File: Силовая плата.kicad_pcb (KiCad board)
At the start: 6 copper layers, 65.7 x 72.2 mm, 57 parts, among them J3 Conn_01x01, J4 Conn_01x01, J5 Conn_01x01, J6 Conn_02x04_Odd_Even, Q1 BSP89, Q2 BSP89, Q3 BSP89, Q4 BSP89, Q5 BSP89, Q6 BSP89, U1 LMV7239M5, U6 AD8210

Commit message: Стартовая версия
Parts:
- removed C11: 56p, Capacitor_SMD:C_0805_2012Metric_Pad1.18x1.45mm_HandSolder
- removed C14, C15, C16, C17, C18, C19, C20, C21: 4.7u, Capacitor_SMD:C_1206_3216Metric_Pad1.33x1.80mm_HandSolder
- removed C2: 1400m, Capacitor_THT:CP_Axial_L30.0mm_D18.0mm_P35.00mm_Horizontal
- removed C5, C7, C9: BS, Capacitor_SMD:C_0805_2012Metric_Pad1.18x1.45mm_HandSolder
- removed C6, C8: 10u, Capacitor_SMD:C_0805_2012Metric_Pad1.18x1.45mm_HandSolder
- removed D1, D2, D5: D_Small, Diode_SMD:D_SOD-323
- removed D3, D4, D6: ADP3110A, Package_DFN_QFN:DFN-8-1EP_3x3mm_P0.65mm_EP1.7x2.05mm
- removed R13, R14, R15, R16, R17, R18: 2.7, Resistor_SMD:R_0805_2012Metric_Pad1.20x1.40mm_HandSolder
- removed R21: 10k, Resistor_SMD:R_0805_2012Metric_Pad1.20x1.40mm_HandSolder
- removed R3, R4: 120, Resistor_SMD:R_0805_2012Metric_Pad1.20x1.40mm_HandSolder
- added J7: A_CTRL, Connector_PinSocket_2.54mm:PinSocket_2x04_P2.54mm_Vertical_SMD, F.Cu at (106.0, 114.3)
- added J9: C_CTRL, Connector_PinSocket_2.54mm:PinSocket_2x04_P2.54mm_Vertical_SMD, F.Cu at (59.7, 113.7)
- added Q10: BSP89, Package_SON:VSONP-8-1EP_5x6_P1.27mm, F.Cu at (87.0, 74.9)
- added Q11: BSP89, Package_SON:VSONP-8-1EP_5x6_P1.27mm, F.Cu at (87.0, 80.6)
- added Q12: BSP89, Package_SON:VSONP-8-1EP_5x6_P1.27mm, F.Cu at (87.0, 86.4)
- added Q13: BSP89, Package_SON:VSONP-8-1EP_5x6_P1.27mm, F.Cu at (68.3, 99.7)
- added Q14: BSP89, Package_SON:VSONP-8-1EP_5x6_P1.27mm, F.Cu at (68.3, 94.0)
- added Q15: BSP89, Package_SON:VSONP-8-1EP_5x6_P1.27mm, F.Cu at (68.3, 88.3)
- added Q16: BSP89, Package_SON:VSONP-8-1EP_5x6_P1.27mm, F.Cu at (98.1, 94.0)
- added Q17: BSP89, Package_SON:VSONP-8-1EP_5x6_P1.27mm, F.Cu at (98.1, 88.3)
- added Q18: BSP89, Package_SON:VSONP-8-1EP_5x6_P1.27mm, F.Cu at (98.1, 82.5)
- added Q19: BSP89, Package_SON:VSONP-8-1EP_5x6_P1.27mm, F.Cu at (79.4, 74.9)
- added Q20: BSP89, Package_SON:VSONP-8-1EP_5x6_P1.27mm, F.Cu at (79.4, 80.6)
- added Q21: BSP89, Package_SON:VSONP-8-1EP_5x6_P1.27mm, F.Cu at (79.4, 86.4)
- added Q22: BSP89, Package_SON:VSONP-8-1EP_5x6_P1.27mm, F.Cu at (60.6, 82.5)
- added Q23: BSP89, Package_SON:VSONP-8-1EP_5x6_P1.27mm, F.Cu at (60.6, 88.3)
- added Q24: BSP89, Package_SON:VSONP-8-1EP_5x6_P1.27mm, F.Cu at (60.6, 94.0)
- added Q7: BSP89, Package_SON:VSONP-8-1EP_5x6_P1.27mm, F.Cu at (105.7, 99.7)
- added Q8: BSP89, Package_SON:VSONP-8-1EP_5x6_P1.27mm, F.Cu at (105.7, 94.0)
- added Q9: BSP89, Package_SON:VSONP-8-1EP_5x6_P1.27mm, F.Cu at (105.7, 88.3)
- added TH1: 10k, Resistor_SMD:R_1206_3216Metric_Pad1.30x1.75mm_HandSolder, B.Cu at (83.2, 75.6)
- C1: footprint Capacitor_THT:CP_Axial_L30.0mm_D18.0mm_P35.00mm_Horizontal -> Capacitor_SMD:CP_Elec_10x12.5
- C10, C12, R10, R11, R5, R6, R7, R8, R9, U6: moved to F.Cu
- C3: value 0.1u -> 100n; moved to F.Cu
- C4: value 10u -> 100n
- J6: value Conn_02x04_Odd_Even -> B_CTRL; footprint Connector_PinHeader_2.54mm:PinHeader_2x04_P2.54mm_Vertical -> Connector_PinSocket_2.54mm:PinSocket_2x02_P2.54mm_Vertical_SMD
- Q1, Q2, Q3, Q4, Q5, Q6: footprint Package_TO_SOT_SMD:TO-263-2 -> Package_SON:VSONP-8-1EP_5x6_P1.27mm
- R2: value 120 -> 10k; moved to F.Cu
- U1: value LMV7239M5 -> AD8603; footprint Package_TO_SOT_SMD:SOT-353_SC-70-5 -> Package_TO_SOT_SMD:TSOT-23-5; moved to F.Cu
- moved C1 66.8 mm to (83.8, 127.0)
- moved U1 61.3 mm to (139.6, 73.8), turned to 0 degrees
- moved C3 55.3 mm to (134.6, 73.1), turned to 0 degrees
- moved R2 54.8 mm to (139.4, 77.5), turned to 0 degrees
- moved C4 50.3 mm to (134.6, 76.1), turned to 0 degrees
- moved J4 37.3 mm to (83.2, 55.8)
- moved R6 35.4 mm to (103.5, 105.4), turned to 90 degrees
- moved Q1 33.0 mm to (105.7, 82.5)
- moved Q2 26.5 mm to (98.1, 99.7), turned to 0 degrees
- moved R7 23.8 mm to (94.6, 105.4), turned to 90 degrees
- moved Q4 23.2 mm to (79.4, 92.1)
- moved J5 22.9 mm to (64.8, 63.4)
- moved Q5 22.5 mm to (68.3, 82.5), turned to 180 degrees
- moved R11 21.6 mm to (57.8, 105.4), turned to 90 degrees
- moved J3 21.1 mm to (101.6, 63.4)
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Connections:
- C12 pad 1: Net-(U1--) -> DC_Measure
- C3 pad 1: +5V -> Net-(U1-+)
- C4 pad 1: GND -> +5V
- C4 pad 2: +12V -> GND
- J6 pad 1: IN_A -> G3
- J6 pad 2: GND -> G4
- J6 pad 3: IN_B -> B
- J6 pad 4: +12V -> GND
- R2 pad 1: Net-(R2-Pad1) -> +5V
- R2 pad 2: Enable -> Net-(U1-+)
- R5 pad 1: Net-(U1--) -> DC_Measure
- R5 pad 2: DC_Measure -> Net-(U6-OUT)
- U1 pad 1: Net-(R2-Pad1) -> Temp_out
- U1 pad 4: Net-(U1--) -> Temp_out
- U6 pad 5: DC_Measure -> Net-(U6-OUT)
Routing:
- net GND: track 52.5 -> 0.00 mm, vias 17 -> 23
- net +5V: track 45.9 -> 0.00 mm, vias 2 -> 0
- net +12V: track 43.1 -> 0.00 mm, vias 5 -> 0
- net DC_Measure: track 32.3 -> 0.00 mm, vias 1 -> 0
- net IN_C: track 31.8 -> 0.00 mm, vias 1 -> 0
- net IN_B: track 30.0 -> 0.00 mm, vias 1 -> 0
- net Enable: track 29.9 -> 0.00 mm, vias 5 -> 0
- net IN_A: track 28.7 -> 0.00 mm, vias 1 -> 0
- net B: track 18.6 -> 0.00 mm, vias 2 -> 8
- net A: track 16.1 -> 0.00 mm, vias 2 -> 8
- net C: track 15.4 -> 0.00 mm, vias 2 -> 7
- net G5: track 5.13 -> 15.6 mm, vias 1 -> 4
- net G1: track 7.80 -> 16.0 mm, vias 1 -> 4
- net Net-(D1-K): track 7.89 -> 0.00 mm
- net G6: track 7.36 -> 15.2 mm, vias 1 -> 4
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- added copper zone on In2.Cu, net G1
- added copper zone on In2.Cu, net G2
- added copper zone on In2.Cu, net G3
- added copper zone on In2.Cu, net G4
- added copper zone on In2.Cu, net G5
- added copper zone on In2.Cu, net G6
- removed copper zone on In2.Cu, net +12V
- removed copper zone on In1.Cu, net A
- removed copper zone on In2.Cu, net A
- removed copper zone on In3.Cu, net A
- removed copper zone on In4.Cu, net A
- removed copper zone on In1.Cu, net B
- removed copper zone on In2.Cu, net B
- removed copper zone on In3.Cu, net B
- removed copper zone on In4.Cu, net B
- removed copper zone on In1.Cu, net C
- removed copper zone on In2.Cu, net C
- removed copper zone on In3.Cu, net C
- removed copper zone on In4.Cu, net C
- removed copper zone on In1.Cu, net Enable
- removed copper zone on F.Cu, net Shunt_1
- removed copper zone on B.Cu, net Shunt_2
- removed copper zone on In1.Cu, net Shunt_2
- removed copper zone on In4.Cu, net Shunt_2
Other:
- board size 65.7 x 72.2 mm -> 66 x 71.8 mm

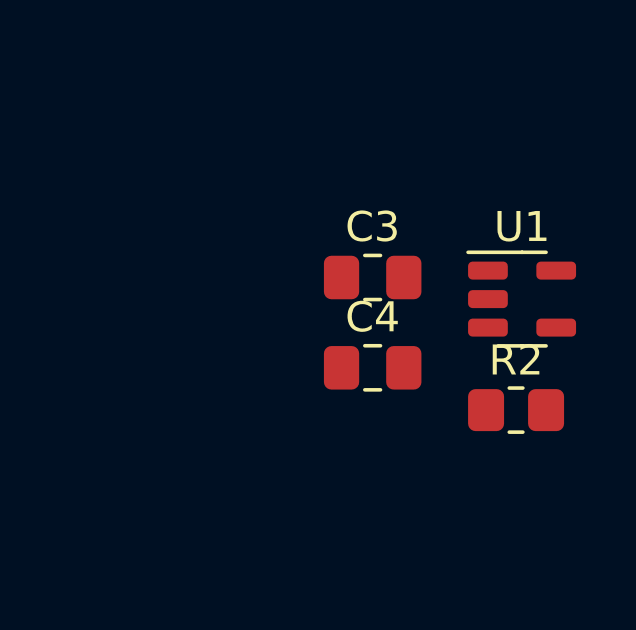
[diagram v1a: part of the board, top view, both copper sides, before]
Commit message: Добавил температурный контур
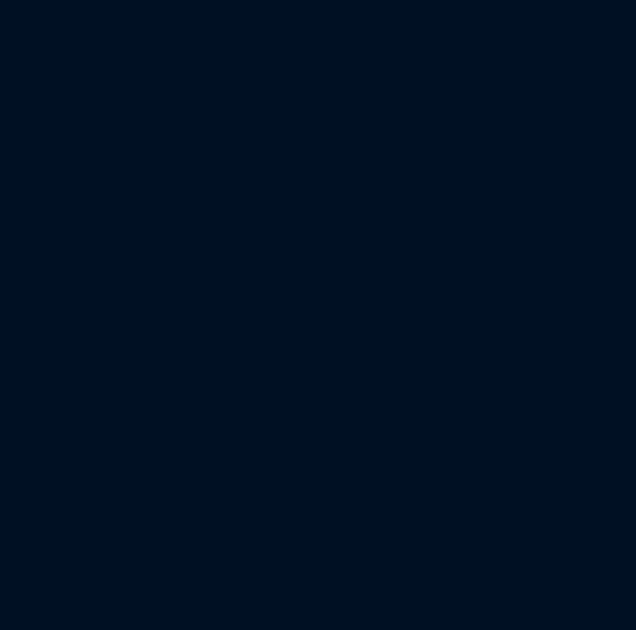
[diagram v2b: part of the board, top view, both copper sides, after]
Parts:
- removed C3, C4: 100n, Capacitor_SMD:C_0805_2012Metric_Pad1.18x1.45mm_HandSolder
- removed R2: 10k, Resistor_SMD:R_0805_2012Metric_Pad1.20x1.40mm_HandSolder
- removed U1: AD8603, Package_TO_SOT_SMD:TSOT-23-5

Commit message: Стартовая версия
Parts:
- removed C1: 1400m, Capacitor_SMD:CP_Elec_10x12.5
- removed C12: 56p, Capacitor_SMD:C_0805_2012Metric_Pad1.18x1.45mm_HandSolder
- removed J7: A_CTRL, Connector_PinSocket_2.54mm:PinSocket_2x04_P2.54mm_Vertical_SMD
- removed Q10, Q11, Q12, Q13, Q14, Q15, Q16, Q17, Q18, Q19, Q20, Q21, Q22, Q23, Q24, Q7, Q8, Q9: BSP89, Package_SON:VSONP-8-1EP_5x6_P1.27mm
- removed R34: R, Shunt_My:TLRS1050
- removed U6: AD8210, Package_SO:SOIC-8_3.9x4.9mm_P1.27mm
- added C11: 100n, Capacitor_SMD:C_0805_2012Metric_Pad1.18x1.45mm_HandSolder, F.Cu at (104.8, 121.9)
- added C2: 0.1u, Capacitor_SMD:C_0805_2012Metric_Pad1.18x1.45mm_HandSolder, F.Cu at (94.2, 116.2)
- added C3: 56p, Capacitor_SMD:C_0805_2012Metric_Pad1.18x1.45mm_HandSolder, F.Cu at (98.4, 117.7)
- added C4: 100n, Capacitor_SMD:C_0805_2012Metric_Pad1.18x1.45mm_HandSolder, F.Cu at (108.6, 127.0)
- added C5: 100n, Capacitor_SMD:C_0805_2012Metric_Pad1.18x1.45mm_HandSolder, F.Cu at (112.2, 121.9)
- added C6: 1500p, Capacitor_THT:C_Rect_L10.0mm_W3.0mm_P7.50mm_FKS3_FKP3, F.Cu at (64.7, 123.2)
- added C7: 1500p, Capacitor_THT:C_Rect_L10.0mm_W3.0mm_P7.50mm_FKS3_FKP3, F.Cu at (57.2, 127.0)
- added C8: 100n, Capacitor_SMD:C_0805_2012Metric_Pad1.18x1.45mm_HandSolder, F.Cu at (93.3, 127.0)
- added C9: 100n, Capacitor_SMD:C_0805_2012Metric_Pad1.18x1.45mm_HandSolder, F.Cu at (97.2, 121.9)
- added R12: 10k, Resistor_SMD:R_0805_2012Metric_Pad1.20x1.40mm_HandSolder, F.Cu at (104.8, 128.3)
- added R2: R, Shunt_My:TLRS1050, F.Cu at (87.0, 106.8)
- added R3: 10k, Resistor_SMD:R_0805_2012Metric_Pad1.20x1.40mm_HandSolder, F.Cu at (104.1, 114.3)
- added R4: 10k, Resistor_SMD:R_0805_2012Metric_Pad1.20x1.40mm_HandSolder, F.Cu at (101.6, 114.3)
- added TH2: 10k, Resistor_SMD:R_1206_3216Metric_Pad1.30x1.75mm_HandSolder, F.Cu at (71.1, 87.0)
- added TH3: 10k, Resistor_SMD:R_1206_3216Metric_Pad1.30x1.75mm_HandSolder, F.Cu at (110.5, 87.0)
- added U1: AD8210, Package_SO:SOIC-8_3.9x4.9mm_P1.27mm, F.Cu at (93.3, 111.1)
- added U2: AD8603, Package_TO_SOT_SMD:TSOT-23-5, F.Cu at (112.3, 125.1)
- added U3: AD8603, Package_TO_SOT_SMD:TSOT-23-5, F.Cu at (97.2, 125.1)
- added U4: AD8603, Package_TO_SOT_SMD:TSOT-23-5, F.Cu at (104.8, 125.1)
- C10: value 0.1u -> 100n
- J6: value B_CTRL -> Conn_01x04; footprint Connector_PinSocket_2.54mm:PinSocket_2x02_P2.54mm_Vertical_SMD -> Connector_PinHeader_2.54mm:PinHeader_1x04_P2.54mm_Vertical
- J9: value C_CTRL -> Conn_01x08; footprint Connector_PinSocket_2.54mm:PinSocket_2x04_P2.54mm_Vertical_SMD -> Connector_PinHeader_2.54mm:PinHeader_1x08_P2.54mm_Vertical
- Q1, Q2, Q3, Q4, Q5, Q6: value BSP89 -> 2N7002; footprint Package_SON:VSONP-8-1EP_5x6_P1.27mm -> MOSFET_My:IPTG007N06NM5ATMA1
- R5: value 120 -> 10k
- R9: value 10k -> 120
- TH1: moved to F.Cu
- moved R10 51.4 mm to (112.0, 128.3), turned to 180 degrees
- moved R11 45.5 mm to (97.2, 128.3), turned to 180 degrees
- moved R6 36.7 mm to (67.9, 114.3)
- moved C10 36.4 mm to (101.0, 127.0)
- moved R7 35.4 mm to (60.3, 114.3), turned to -90 degrees
- moved R8 34.0 mm to (57.8, 114.3), turned to 90 degrees
- moved R9 27.7 mm to (94.3, 118.7), turned to 180 degrees
- moved J6 24.1 mm to (102.1, 118.4), turned to 90 degrees
- moved Q5 23.3 mm to (63.5, 105.3)
- moved Q1 23.0 mm to (102.9, 105.3)
- moved Q2 15.3 mm to (102.9, 85.1)
- moved Q4 15.1 mm to (83.2, 77.5)
- moved Q6 14.7 mm to (63.5, 85.3)
- moved TH1 8.52 mm to (90.8, 79.4), turned to -90 degrees
- moved R1 6.90 mm to (79.4, 106.8)
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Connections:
- C10 pad 1: +5V -> Net-(U4-+)
- J6 pad 1: G3 -> G1
- J6 pad 2: G4 -> A
- J6 pad 3: B -> G2
- J9 pad 1: G5 -> G6
- J9 pad 2: G6 -> GND
- J9 pad 3: C -> G5
- J9 pad 4: GND -> C
- J9 pad 5: DC_Measure -> G4
- J9 pad 7: +5V -> G3
- J9 pad 8: GND -> B
- Q1 pad 2: Shunt_2 -> A
- Q1 pad 3: A -> Shunt_2
- Q2 pad 2: A -> GND
- Q2 pad 3: GND -> A
- Q3 pad 2: Shunt_2 -> B
- Q3 pad 3: B -> Shunt_2
- Q4 pad 2: B -> GND
- Q4 pad 3: GND -> B
- Q5 pad 2: Shunt_2 -> C
- Q5 pad 3: C -> Shunt_2
- Q6 pad 2: C -> GND
- Q6 pad 3: GND -> C
- R10 pad 1: C -> +5V
- R10 pad 2: G5 -> Net-(U2-+)
- R11 pad 1: GND -> +5V
- R11 pad 2: G6 -> Net-(U3-+)
- R5 pad 1: DC_Measure -> B
- R5 pad 2: Net-(U6-OUT) -> G3
- R6 pad 1: A -> GND
- R6 pad 2: G1 -> G4
- R7 pad 1: GND -> C
- R7 pad 2: G2 -> G5
- R8 pad 1: B -> GND
- R8 pad 2: G3 -> G6
- R9 pad 1: GND -> DC_Measure
- R9 pad 2: G4 -> Net-(U1-OUT)
- TH1 pad 1: Net-(U1-+) -> Net-(U2-+)
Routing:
- net G4: track 14.2 -> 36.5 mm, vias 4 -> 1
- net GND: track 0.00 -> 16.6 mm, vias 23 -> 47
- net G6: track 15.2 -> 29.1 mm, vias 4 -> 1
- net G3: track 14.3 -> 25.8 mm, vias 4 -> 1
- net Shunt_1: track 0.00 -> 11.2 mm
- net B: track 0.00 -> 6.97 mm, vias 8 -> 0
- net C: track 0.00 -> 6.97 mm, vias 7 -> 0
- net G2: track 15.1 -> 21.8 mm, vias 4 -> 1
- net Net-(U1-OUT): track 0.00 -> 5.93 mm
- net +5V: track 0.00 -> 4.07 mm
- net DC_Measure: track 0.00 -> 3.08 mm
- net G5: track 15.6 -> 18.4 mm, vias 4 -> 1
- net Net-(U4-+): track 0.00 -> 2.52 mm, vias 0 -> 1
- net Net-(U3-+): track 0.00 -> 1.62 mm, vias 0 -> 1
- net Net-(U2-+): track 0.00 -> 1.62 mm, vias 0 -> 1
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- added copper zone on F.Cu, net Shunt_1
- removed copper zone on B.Cu, net A
- removed copper zone on B.Cu, net B
- removed copper zone on B.Cu, net C
- removed copper zone on In2.Cu, net G1
- removed copper zone on In2.Cu, net G2
- removed copper zone on In2.Cu, net G3
- removed copper zone on In2.Cu, net G4
- removed copper zone on In2.Cu, net G5
- removed copper zone on In2.Cu, net G6
- removed copper zone on B.Cu, net GND
